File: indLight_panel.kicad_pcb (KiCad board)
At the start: 2 copper layers, 48 x 88 mm, 37 parts, among them P1 TTL_232R_3V3, P2 CONN_01X02, P3 CONN_01X04, P4 CONN_01X04, U1 REG1117, U2 LT1933, U3 SN74LVC2G17, U4 esp8266_esp-02

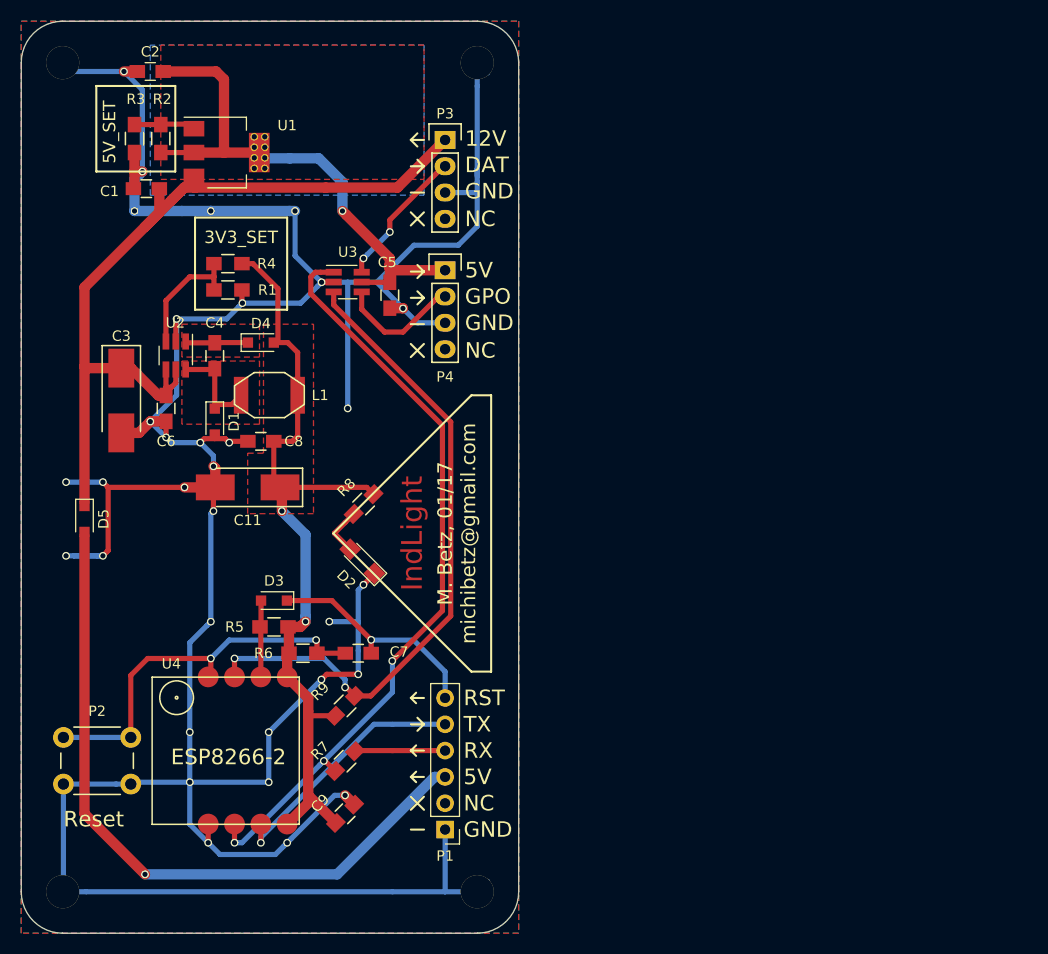
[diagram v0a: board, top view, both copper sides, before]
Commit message: REV1. Added top lid, better DCDC, gerb. Ordered
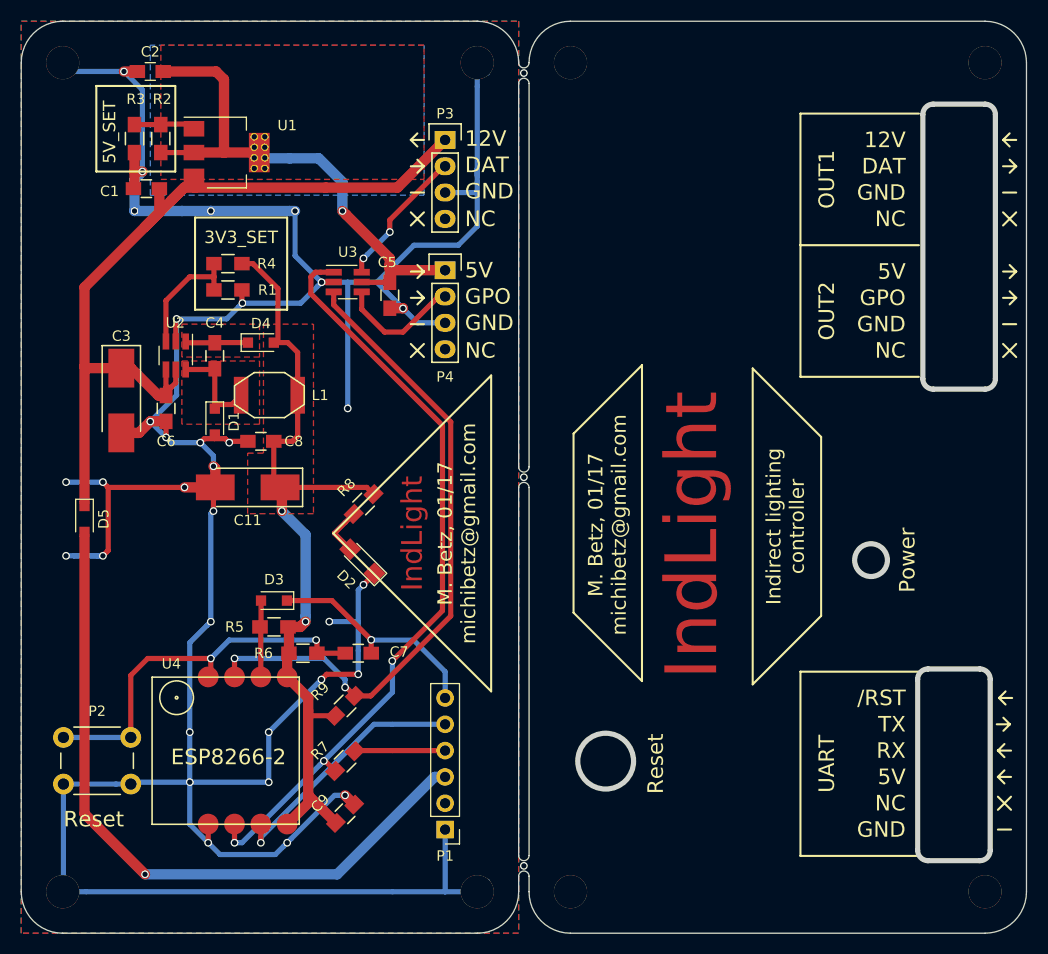
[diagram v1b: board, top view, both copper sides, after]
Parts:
- added W1: TEST_1P, Mounting_Holes:MountingHole_3.2mm_M3, F.Cu at (101.0, 53.0)
- added W2: TEST_1P, Mounting_Holes:MountingHole_3.2mm_M3, F.Cu at (141.0, 53.0)
- added W3: TEST_1P, Mounting_Holes:MountingHole_3.2mm_M3, F.Cu at (101.0, 133.0)
- added W4: TEST_1P, Mounting_Holes:MountingHole_3.2mm_M3, F.Cu at (141.0, 133.0)
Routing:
- net (no net): vias 0 -> 3
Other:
- board size 48 x 88 mm -> 97 x 88 mm
- board text added: "/RST"
- board text added: "Indirect lighting controller"
- board text added: "OUT1"
- board text added: "OUT2"
- board text added: "Power"
- board text added: "UART"
- board text removed: "RST"
